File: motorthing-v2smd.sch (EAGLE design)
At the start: 16 parts, among them IC1 MAX485, IC2 4N25M, IC3 wemos D1 Mini, IC4 7805TV, J1 DCJ0202LARGE_VIA, X1 1501_0LARGE_VIA

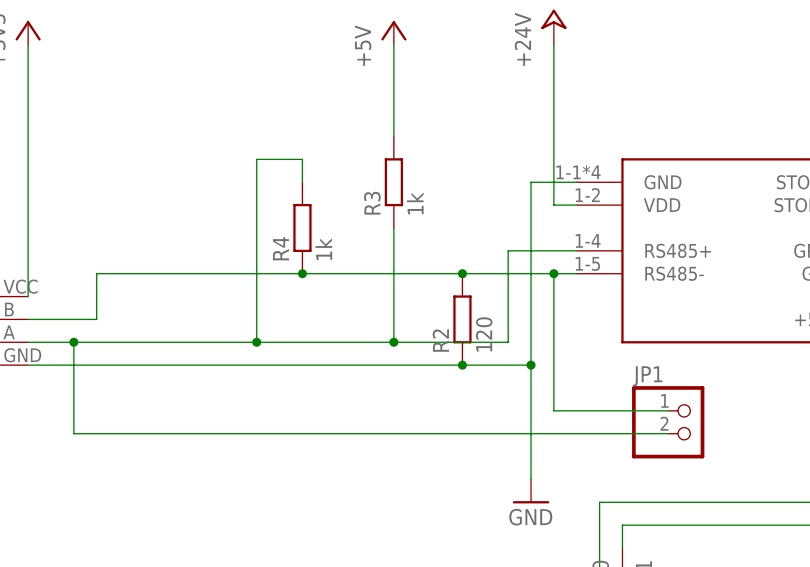
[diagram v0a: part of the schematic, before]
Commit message: fix resistor values
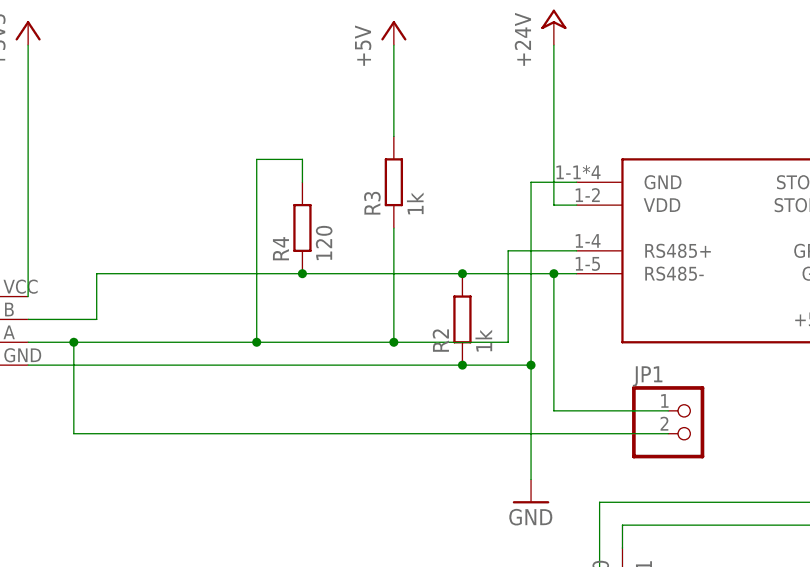
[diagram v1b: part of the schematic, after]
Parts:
- R2: value 120 -> 1k
- R4: value 1k -> 120
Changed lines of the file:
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@@
 <part name="GND4" library="supply1" deviceset="GND" device=""/>
 <part name="JP3" library="pinhead" deviceset="PINHD-1X2" device=""/>
-<part name="R2" library="rcl" deviceset="R-EU_" device="0207/10" value="120"/>
+<part name="R2" library="rcl" deviceset="R-EU_" device="0207/10" value="1k"/>
 <part name="R3" library="rcl" deviceset="R-EU_" device="0207/10" value="1k"/>
-<part name="R4" library="rcl" deviceset="R-EU_" device="0207/10" value="1k"/>
+<part name="R4" library="rcl" deviceset="R-EU_" device="0207/10" value="120"/>
 <part name="P+5" library="supply1" deviceset="+5V" device=""/>
 </parts>
